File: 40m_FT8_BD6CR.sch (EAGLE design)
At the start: 49 parts, among them J1 AUDIO-JACK2KIT, J2 AUDIO-JACK2KIT, Q1 2N3904, Q2 2N3904, Q3 2N3904, Q4 2N3904

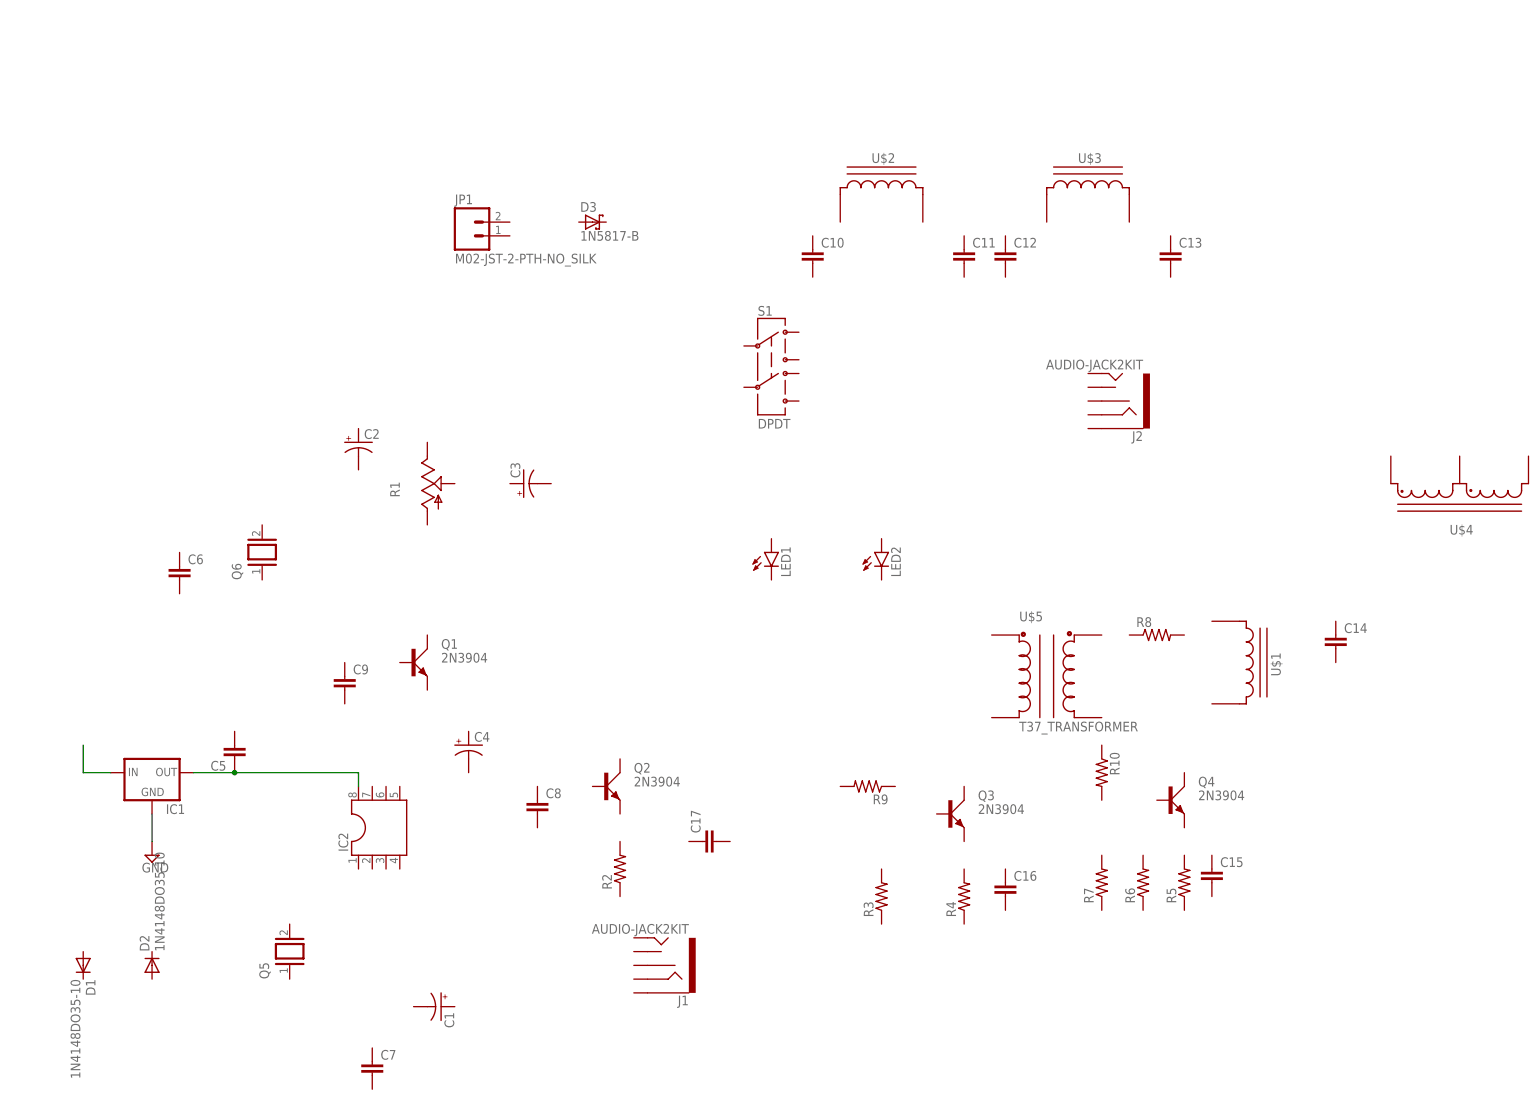
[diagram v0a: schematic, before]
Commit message: First version done and ready for review
Changes to be committed:
       new file:   40m_FT8_BD6CR.pdf
       modified:   40m_FT8_BD6CR.s#1
       new file:   40m_FT8_BD6CR.s#2
       new file:   40m_FT8_BD6CR.s#3
       new file:   40m_FT8_BD6CR.s#4
       new file:   40m_FT8_BD6CR.s#5
       new file:   40m_FT8_BD6CR.s#6
       new file:   40m_FT8_BD6CR.s#7
       new file:   40m_FT8_BD6CR.s#8
       new file:   40m_FT8_BD6CR.s#9
       modified:   40m_FT8_BD6CR.sch
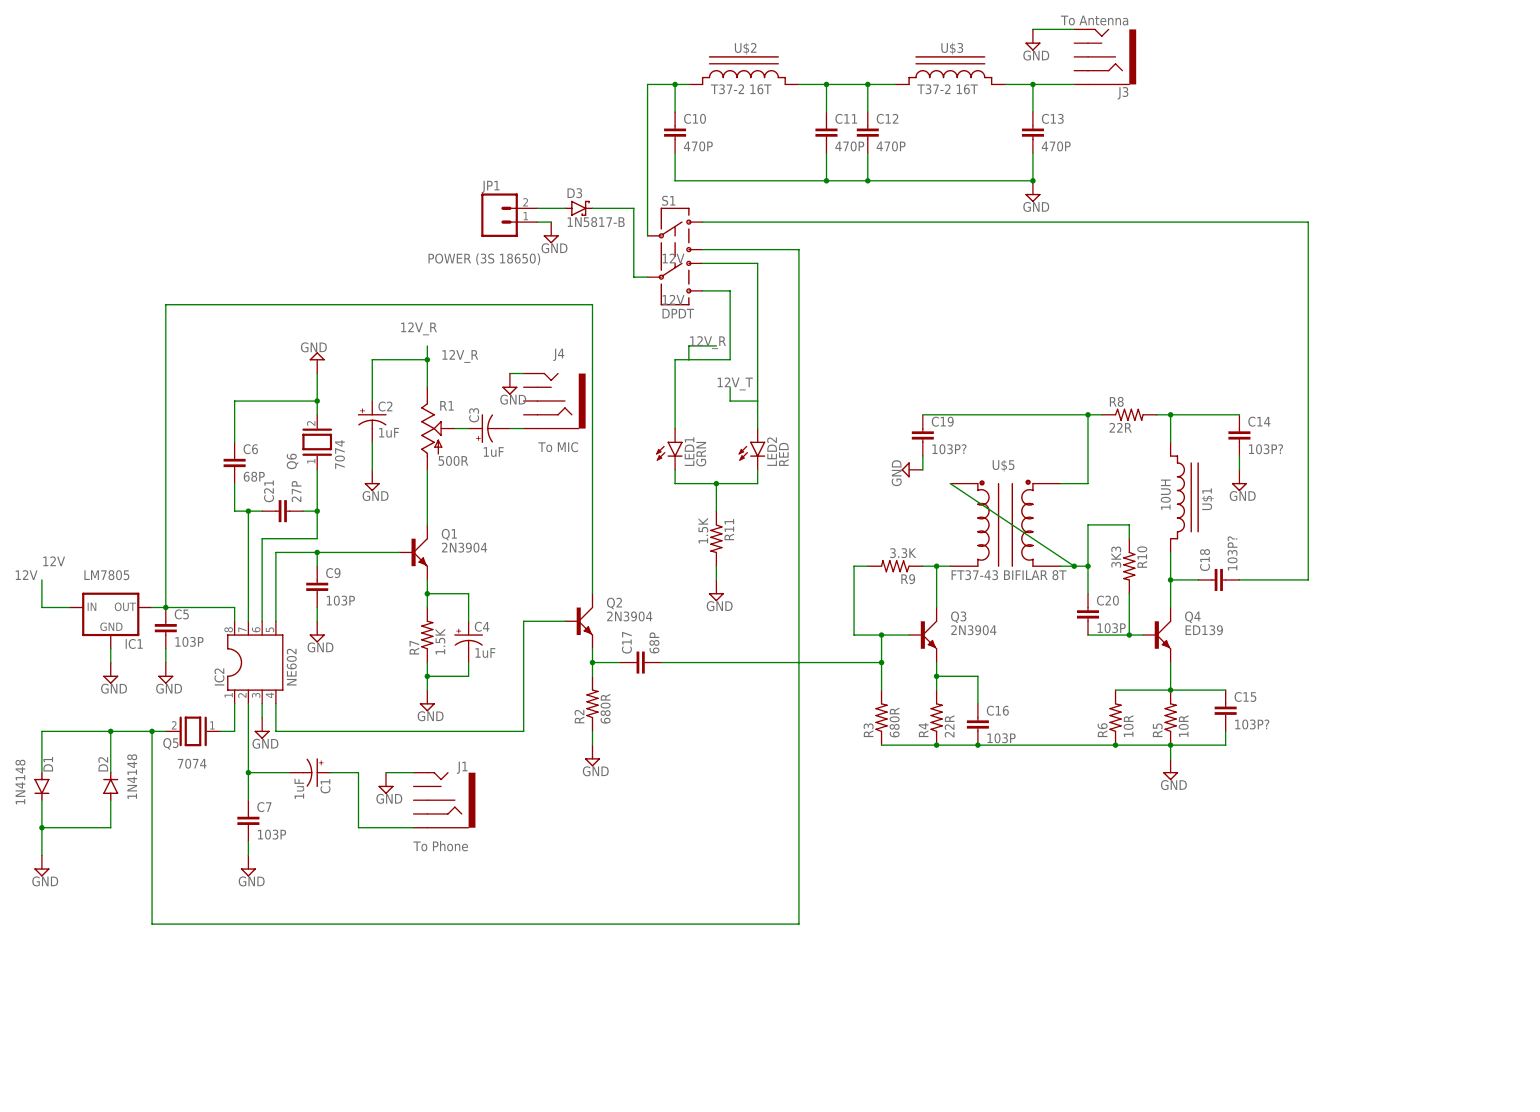
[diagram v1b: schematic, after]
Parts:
- removed C8: (no value), rcl:C-EU050-025X075
- removed J2: AUDIO-JACK2KIT, SparkFun-Connectors:AUDIO-JACK2KIT
- removed U$4: (no value), toroid:T37_AUTOTRANSFORMER
- added C18, C19: 103P?, rcl:C-EU050-025X075
- added C20: 103P, rcl:C-EU050-025X075
- added C21: 27P, rcl:C-EU050-025X075
- added J3: To Antenna, SparkFun-Connectors:AUDIO-JACK2KIT
- added J4: To MIC, SparkFun-Connectors:AUDIO-JACK2KIT
- added R11: 1.5K, SparkFun-Resistors:RESISTOR0402
- C1, C2, C3, C4: value (none) -> 1uF
- C10, C11, C12, C13: value (none) -> 470P
- C14, C15: value (none) -> 103P?
- C16, C5, C7, C9: value (none) -> 103P
- C17, C6: value (none) -> 68P
- D1, D2: value 1N4148DO35-10 -> 1N4148
- IC1: value (none) -> LM7805
- IC2: value (none) -> NE602
- J1: value AUDIO-JACK2KIT -> To Phone
- JP1: value M02-JST-2-PTH-NO_SILK -> POWER (3S 18650)
- LED1: value (none) -> GRN
- LED2: value (none) -> RED
- Q4: value 2N3904 -> ED139
- Q5, Q6: value (none) -> 7074
- R1: value (none) -> 500R
- R10: value (none) -> 3K3; device SparkFun-Resistors:RESISTORPTH-1/4W -> SparkFun-Resistors:RESISTOR0402
- R2, R3: value (none) -> 680R; device SparkFun-Resistors:RESISTORPTH-1/4W -> SparkFun-Resistors:RESISTOR0402
- R4, R8: value (none) -> 22R; device SparkFun-Resistors:RESISTORPTH-1/4W -> SparkFun-Resistors:RESISTOR0402
- R5, R6: value (none) -> 10R; device SparkFun-Resistors:RESISTORPTH-1/4W -> SparkFun-Resistors:RESISTOR0402
- R7: value (none) -> 1.5K; device SparkFun-Resistors:RESISTORPTH-1/4W -> SparkFun-Resistors:RESISTOR0402
- R9: value (none) -> 3.3K; device SparkFun-Resistors:RESISTORPTH-1/4W -> SparkFun-Resistors:RESISTOR0402
- U$1: value T37_INDUCTOR -> 10uH; device toroid:T37_INDUCTOR -> toroid:T37_INDUCTOR_FLAT; 10UH (none) -> 10UH
- U$2: value T37_INDUCTOR -> T37-2 16T; device toroid:T37_INDUCTOR -> toroid:T37_INDUCTOR_FLAT; T37-2_16T (none) -> T37-2 16T
- U$3: value T37_INDUCTOR -> T37_INDUCTOR_FLAT; device toroid:T37_INDUCTOR -> toroid:T37_INDUCTOR_FLAT; T37-2_16T (none) -> T37-2 16T
- U$5: value T37_TRANSFORMER -> FT37-43 BIFILAR 8T
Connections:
- new net 12V: D3.C, IC1.IN, S1.5
- new net 12V_R: C2.+, LED1.A, R1.E, S1.6
- new net 12V_T: LED2.A, S1.4
- new net N$10: C14.1, R8.2, U$1.CB
- new net N$11: C19.1, R8.1, U$5.C2B
- new net N$12: C15.1, Q4.E, R5.2, R6.2
- new net N$13: C20.1, R10.1, U$5.C1B, U$5.C2A
- new net N$14: C20.2, Q4.B, R10.2
- new net N$15: LED1.C, LED2.C, R11.1
- new net N$16: Q3.C, R9.1, U$5.C1A
- new net N$17: C17.2, Q3.B, R3.2, R9.2
- new net N$18: C16.1, Q3.E, R4.2
- new net N$19: C17.1, Q2.E, R2.2
- new net N$20: C3.-, J4.SLEEVE
- new net N$21: C9.1, IC2.5, Q1.B
- new net N$22: Q1.C, R1.A
- new net N$23: IC2.1, Q5.1
- new net N$24: C21.1, C6.2, IC2.7
- new net N$25: C21.2, IC2.6, Q6.1
- new net N$26: D1.A, D2.C, Q5.2, S1.3
- new net N$27: C1.+, J1.SLEEVE
- new net N$28: C1.-, C7.1, IC2.2
- new net N$29: C4.+, Q1.E, R7.2
- new net N$3: C13.1, J3.SLEEVE, U$3.CA
- new net N$30: IC2.4, Q2.B
- new net N$31: C18.2, S1.1
- new net N$4: C11.1, C12.1, U$2.CA, U$3.CB
- new net N$5: C10.1, S1.2, U$2.CB
- new net N$6: D3.A, JP1.2
- new net N$9: C18.1, Q4.C, U$1.CA
- net GND: now also C10.2, C11.2, C12.2, C13.2, C14.2, C15.2, C16.2, C19.2, C2.-, C4.-, C5.2, C6.1, C7.2, C9.2, D1.C, D2.A, IC2.3, J1.TIP, J3.TIP, J4.TIP, JP1.1, Q6.2, R11.2, R2.1, R3.1, R4.1, R5.1, R6.1, R7.1
- net N$1: now also C3.+, R1.S; no longer IC1.IN
- net N$2: now also Q2.C
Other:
- moved on the sheet: C1, C10, C11, C12, C13, C14, C15, C16, C17, C2, C3, C4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

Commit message: Updated schematic and added the board layout
Updated schematic and added the board layout
1. I found I was missing a resistor (R7 22R)
2. I removed all the audio/mic jacks and replaced them with JST-XH 2 pin connectors so the audio/mic jacks can be connected to a case of some sort.
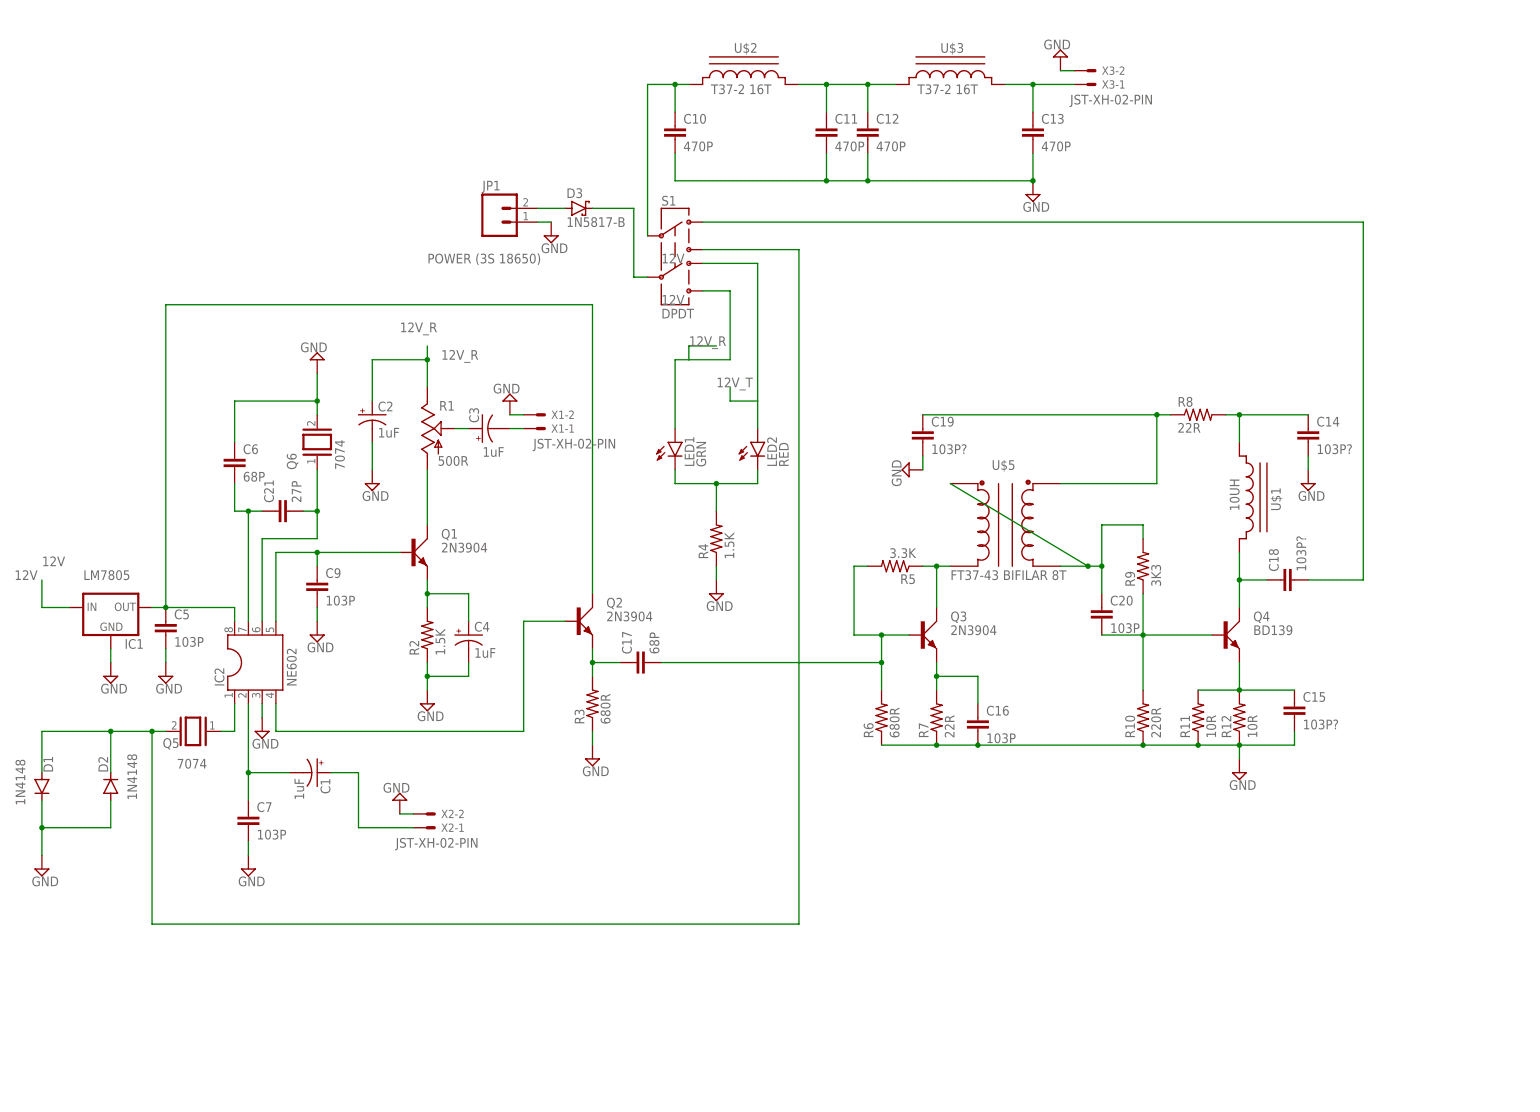
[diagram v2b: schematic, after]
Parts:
- removed J1: To Phone, SparkFun-Connectors:AUDIO-JACK2KIT
- removed J3: To Antenna, SparkFun-Connectors:AUDIO-JACK2KIT
- removed J4: To MIC, SparkFun-Connectors:AUDIO-JACK2KIT
- added R12: 10R, rcl:R-US_0207/10
- added X1, X2, X3: JST-XH-02-PIN, Rembrandt Electronics - JST XH Connectors v1-0:JST-XH-02-PIN-LONG-PAD
- Q4: value ED139 -> BD139
- R10: value 3K3 -> 220R; device SparkFun-Resistors:RESISTOR0402 -> rcl:R-US_0207/10
- R11: value 1.5K -> 10R; device SparkFun-Resistors:RESISTOR0402 -> rcl:R-US_0207/10
- R2: value 680R -> 1.5K; device SparkFun-Resistors:RESISTOR0402 -> rcl:R-US_0207/10
- R3, R8: device SparkFun-Resistors:RESISTOR0402 -> rcl:R-US_0207/10
- R4: value 22R -> 1.5K; device SparkFun-Resistors:RESISTOR0402 -> rcl:R-US_0207/10
- R5: value 10R -> 3.3K; device SparkFun-Resistors:RESISTOR0402 -> rcl:R-US_0207/10
- R6: value 10R -> 680R; device SparkFun-Resistors:RESISTOR0402 -> rcl:R-US_0207/10
- R7: value 1.5K -> 22R; device SparkFun-Resistors:RESISTOR0402 -> rcl:R-US_0207/10
- R9: value 3.3K -> 3K3; device SparkFun-Resistors:RESISTOR0402 -> rcl:R-US_0207/10
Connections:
- removed net N$12: C15.1, Q4.E, R5.2, R6.2
- removed net N$20: C3.-, J4.SLEEVE
- new net N$33: C15.1, Q4.E, R11.2, R12.2
- new net N$7: C3.-, X1-1.S
- net GND: now also R10.1, R11.1, R12.1, X1-2.S, X2-2.S, X3-2.S; no longer J1.TIP, J3.TIP, J4.TIP, R11.2, R5.1
- net N$13: now also R9.2; no longer R10.1
- net N$14: now also R9.1
- net N$15: now also R4.2; no longer R11.1
- net N$16: now also R5.1; no longer R9.1
- net N$17: now also R5.2, R6.2; no longer R3.2, R9.2
- net N$18: now also R7.2; no longer R4.2
- net N$19: now also R3.2; no longer R2.2
- net N$27: now also X2-1.S; no longer J1.SLEEVE
- net N$29: now also R2.2; no longer R7.2
- net N$3: now also X3-1.S; no longer J3.SLEEVE
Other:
- moved on the sheet: C14, C15, C18, C20, Q4, R10, R11, R2, R3, R4, R5, R6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
